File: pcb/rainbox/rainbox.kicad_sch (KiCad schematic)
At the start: 14 parts, among them J1 USB_C_Receptacle_USB2.0_14P, J2 Conn_01x04_Pin, U1 ESP32-S3-WROOM-2, U2 LM3940IMPX-3.3/NOPB, U3 ESC, U4 TMC2240_Module

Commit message: more kicad additions and research
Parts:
- added C6, C7: 0.1uF, symbol Device:C_Small
- added J3: Conn_01x02_Pin, symbol Connector:Conn_01x02_Pin
- added J4: Conn_01x02_Socket, Connector_PinSocket_2.54mm:PinSocket_1x02_P2.54mm_Vertical, symbol Connector:Conn_01x02_Socket
- added R4: 400Ω, symbol Device:R_Small
- added R5: 20kΩ, symbol Device:R_Small
- added U5, U6: WaterSensor_Module, Connector_PinHeader_2.54mm:PinHeader_1x03_P2.54mm_Vertical, symbol 1_udu_lib:Water_Sensor_Module
- added U7: Neopixel_Strip_Module, Connector_PinHeader_2.54mm:PinHeader_1x03_P2.54mm_Vertical, symbol 1_udu_lib:Neopixel_Strip_Module
- added U8: Ultrasonic_Atomizer_Module, Connector_PinHeader_2.54mm:PinHeader_1x03_P2.54mm_Vertical, symbol 1_udu_lib:Ultrasonic_Atomizer_Module
- added U9: TPS2113ADRBR, EasyEDA:SON-8_L3.0-W3.0-P0.65-LS3.0-BL-EP, symbol EasyEDA:TPS2113ADRBR
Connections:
- net +3.3V: now also U5.2 (3V3), U6.2 (3V3), U8.2 (3v3)
- net +5V: now also U7.2 (5v), U9.7 (OUT); no longer J1.A4 (VBUS), J1.A9 (VBUS), J1.B4 (VBUS), J1.B9 (VBUS)
- net D+: now also U1.14 (USB_D+/IO20)
- net D-: now also U1.13 (USB_D-/IO19)
- net GND: now also C6.1, C7.1, J3.1 (Pin_1), J4.2 (Pin_2), R4.1, R5.1, U5.3 (GND), U6.3 (GND), U7.3 (GND), U8.3 (GND), U9.2 (~{EN}), U9.5 (GND), U9.9 (EP); no longer U4.3 (EN)
- net DIR: now reaches U4.10 (DIR)
- net DIR: now also U1.6 (IO6)
- net at U4.18 (VM): now also J3.2 (Pin_2)
- net MOSI: now reaches U4.4 (MOSI)
- net MOSI: now also U1.18 (IO10)
- net SPI_CLK: now reaches U4.5 (SPI_CLK)
- net SPI_CLK: now also U1.19 (IO11)
- net CS: now reaches U4.6 (CS)
- net CS: now also U1.20 (IO12)
- net MISO: now reaches U4.7 (MISO)
- net MISO: now also U1.21 (IO13)
- net STEP: now reaches U4.9 (STEP)
- net STEP: now also U1.5 (IO5)
- net RGB: now reaches U1.12 (IO8)
- net RGB: now also U7.1 (Din)
- net Mist: now reaches U1.17 (IO9)
- net Mist: now also U8.1 (Signal)
- net S1Water: now reaches U1.38 (IO2)
- net S1Water: now also U5.1 (Signal)
- net ENABLE: now reaches U1.4 (IO4)
- net ENABLE: now also U4.3 (EN)
- net S2Water: now reaches U1.7 (IO7)
- net S2Water: now also U6.1 (Signal)
- new net: R4.2, U9.4 (ILIM)
- new net: R5.2, U9.3 (VSNS)
- new net 5V_BUCKDC: C7.2, J4.1 (Pin_1), U9.8 (IN1)
- new net 5V_VBUS: C6.2, J1.A4 (VBUS), J1.A9 (VBUS), J1.B4 (VBUS), J1.B9 (VBUS), U9.6 (IN2)
- no-connect marks 1 -> 8
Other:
- note added: "24v->5v dc dc buck converter"
- note added: "mist generator"
- note added: "neopixels"
- note added: "power management/mux"
- note added: "stepper motor"
- note added: "water sensors"
- moved on the sheet: J2

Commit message: update pcb
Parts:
- added C8, C9: 0.1uF, Capacitor_SMD:C_0603_1608Metric, symbol Device:C_Small
- added D1, D2: WS2812B, LED_SMD:LED_WS2812B_PLCC4_5.0x5.0mm_P3.2mm, symbol LED:WS2812B
- added SW1, SW2: SW_Push, Button_Switch_THT:SW_PUSH_6mm, symbol Switch:SW_Push
- added TP1, TP2, TP3: Mount Screw M3, MountingHole:MountingHole_3.2mm_M3_Pad_Via, symbol Connector:TestPoint
- added U10: USBLC6-2P6, Package_TO_SOT_SMD:SOT-666, symbol Power_Protection:USBLC6-2P6
- C1, C2, C3, C4, C5, C6, C7: footprint (none) -> Capacitor_SMD:C_0603_1608Metric
- J1: footprint (none) -> Snapeda:USB4105-GF-A_GCT_USB4105-GF-A
- J2: footprint (none) -> Connector_PinHeader_2.54mm:PinHeader_1x04_P2.54mm_Vertical
- J3: footprint (none) -> TerminalBlock_Phoenix:TerminalBlock_Phoenix_PT-1,5-2-5.0-H_1x02_P5.00mm_Horizontal
- R1, R2, R3, R4, R5: footprint (none) -> Resistor_SMD:R_0603_1608Metric
- U4: footprint (none) -> 1_udu_lib:tmc2240_module
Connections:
- net +3.3V: now also D1.1 (VDD), D2.1 (VDD)
- net 5V_VBUS: now also U10.5 (VBUS)
- net D+: now also U10.4 (I/O2); no longer J1.A6 (D+), J1.B6 (D+)
- net D-: now also U10.6 (I/O1); no longer J1.A7 (D-), J1.B7 (D-)
- net GND: now also C8.2, C9.2, D1.3 (VSS), D2.3 (VSS), SW1.2, SW2.2, TP1.1, TP2.1, TP3.1, U10.2 (GND)
- net EN_RESET: now reaches C3.2, R1.2, U1.3 (EN)
- net EN_RESET: now also C8.1, SW1.1
- net NEOPIXELS: now reaches U1.11 (IO18)
- net NEOPIXELS: now also D1.4 (DIN)
- net BOOT: now reaches U1.27 (IO0)
- net BOOT: now also C9.1, SW2.1
- new net: J1.A6 (D+), J1.B6 (D+), U10.3 (I/O2)
- new net: J1.A7 (D-), J1.B7 (D-), U10.1 (I/O1)
- new net: D1.2 (DOUT), D2.4 (DIN)
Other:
- note added: "boot and reset buttons"
- note added: "mounting screws"

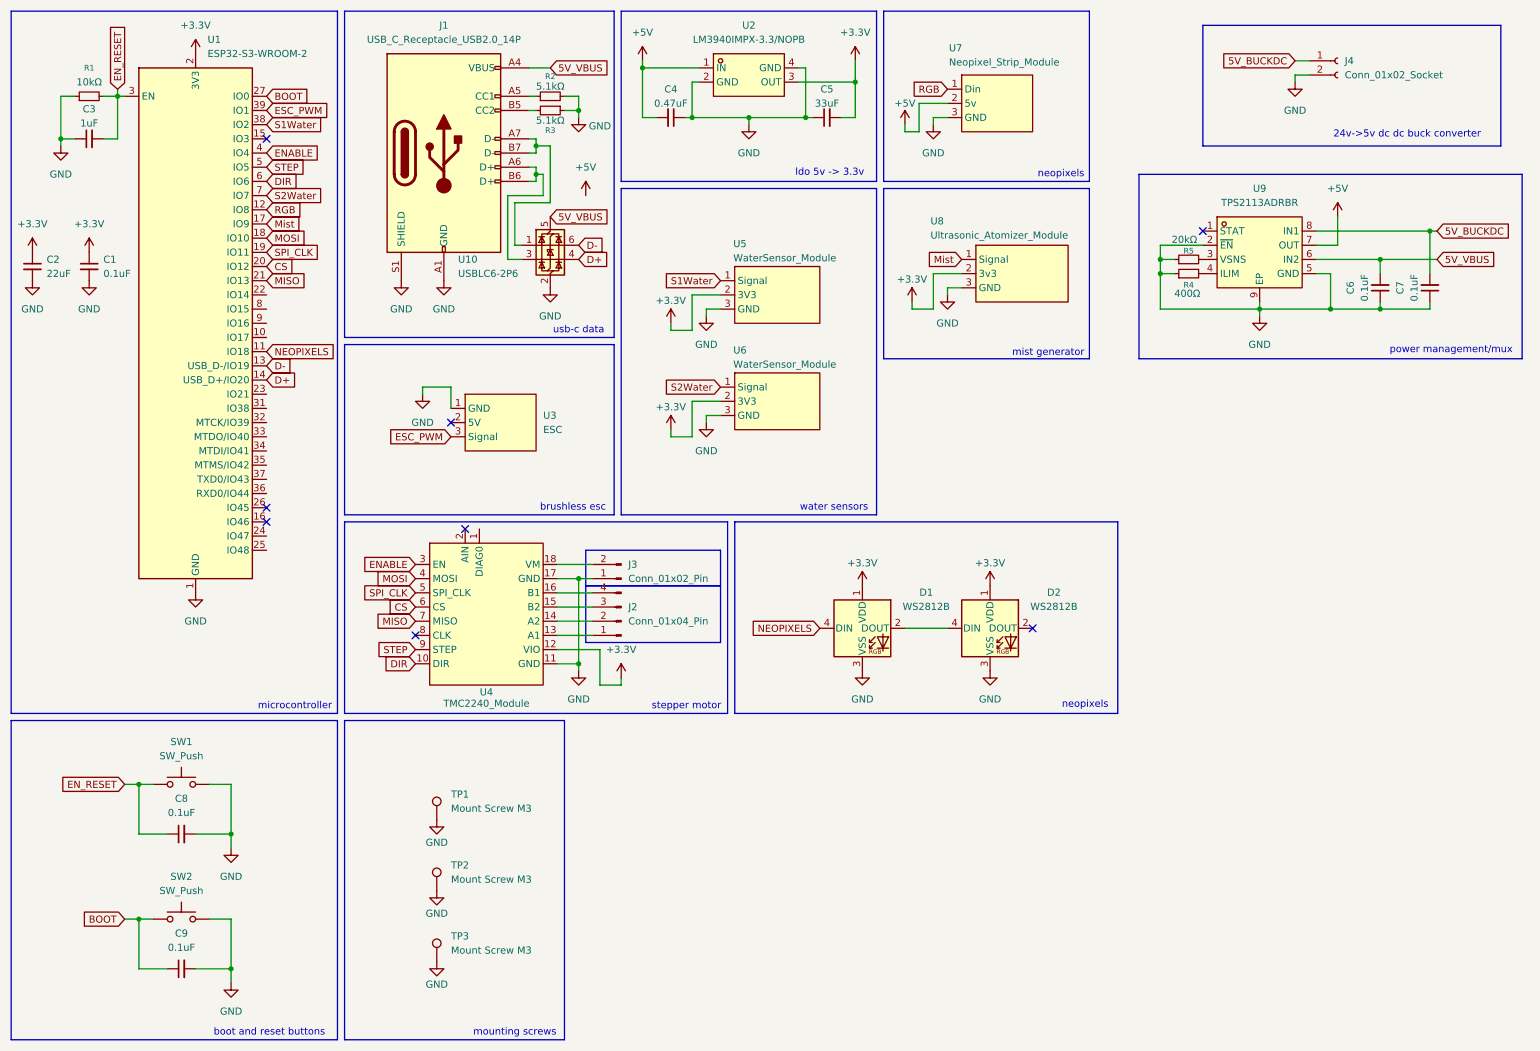
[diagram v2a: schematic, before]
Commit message: replace esc controller with dc motor ic
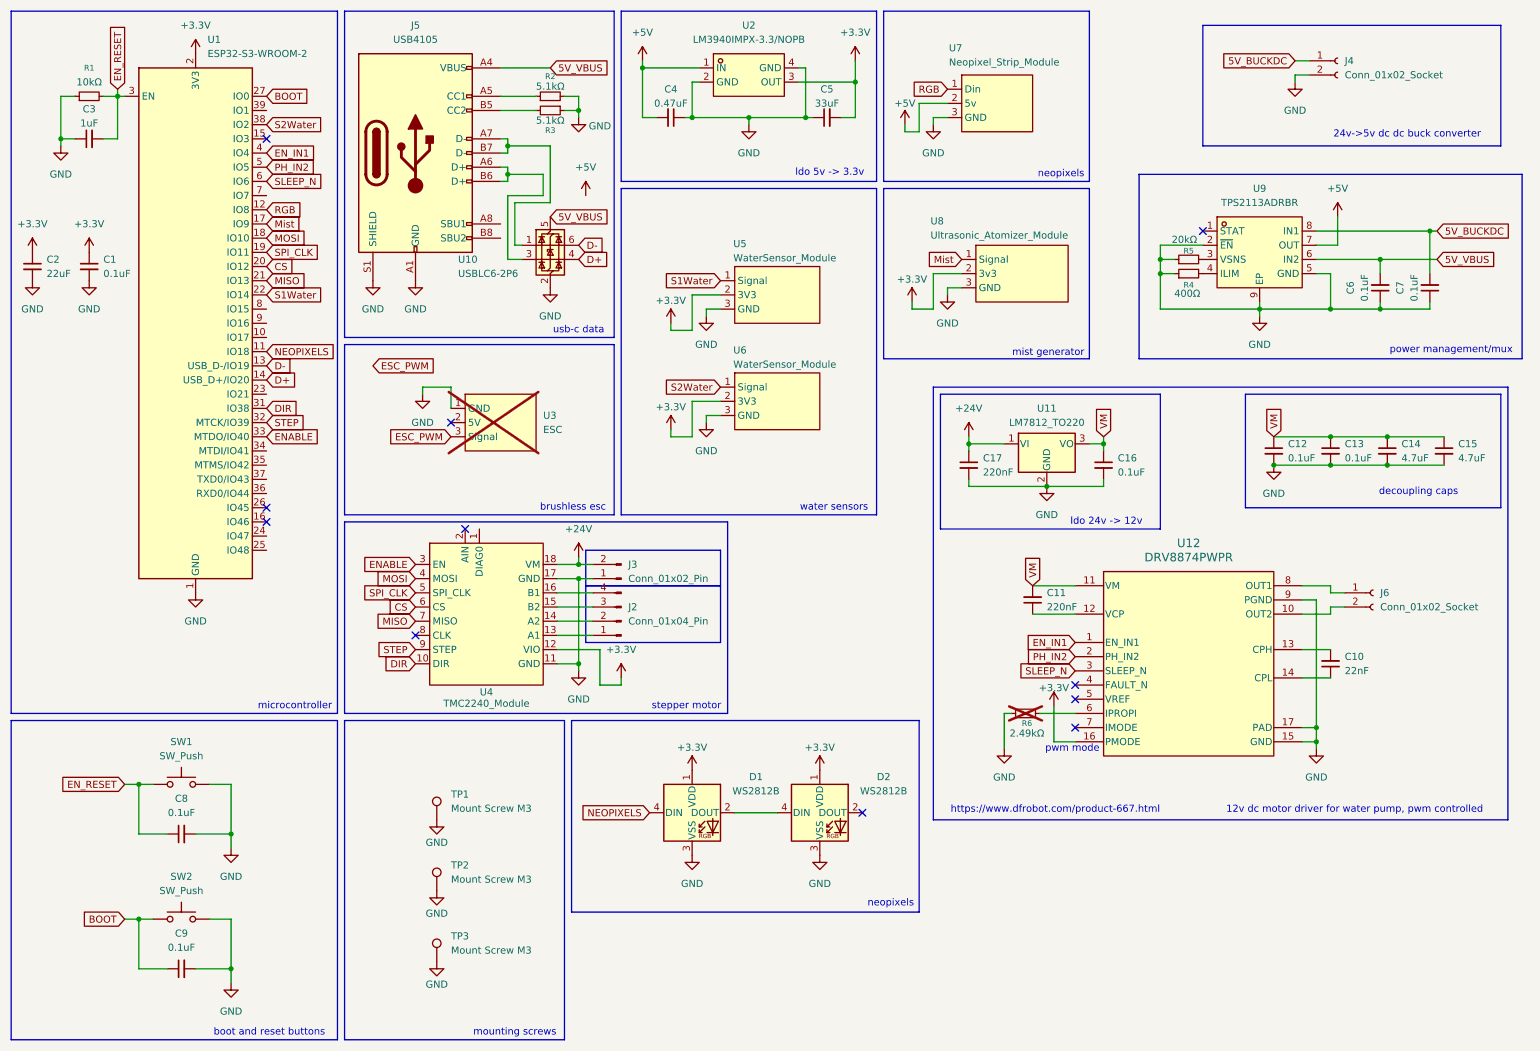
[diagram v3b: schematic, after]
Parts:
- removed J1: USB_C_Receptacle_USB2.0_14P, Snapeda:USB4105-GF-A_GCT_USB4105-GF-A, symbol Connector:USB_C_Receptacle_USB2.0_14P
- added C10: 22nF, Capacitor_SMD:C_0603_1608Metric, symbol Device:C_Small
- added C11, C17: 220nF, Capacitor_SMD:C_0603_1608Metric, symbol Device:C_Small
- added C12, C13, C16: 0.1uF, Capacitor_SMD:C_0603_1608Metric, symbol Device:C_Small
- added C14, C15: 4.7uF, Capacitor_SMD:C_0603_1608Metric, symbol Device:C_Small
- added J5: USB4105, Connector_USB:USB_C_Receptacle_GCT_USB4105-xx-A_16P_TopMnt_Horizontal, symbol Connector:USB_C_Receptacle_USB2.0_16P
- added J6: Conn_01x02_Socket, TerminalBlock_Phoenix:TerminalBlock_Phoenix_PT-1,5-2-5.0-H_1x02_P5.00mm_Horizontal, symbol Connector:Conn_01x02_Socket
- added R6: 2.49kΩ, Resistor_SMD:R_0603_1608Metric, symbol Device:R_Small
- added U11: LM7812_TO220, Package_TO_SOT_THT:TO-220-3_Vertical, symbol Regulator_Linear:LM7812_TO220
- added U12: DRV8874PWPR, 1_udu_lib:PWP0016J_N, symbol drv8874:DRV8874PWPR
- U3: now not fitted; now left out of the parts list
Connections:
- net +3.3V: now also U12.16 (PMODE)
- net 5V_VBUS: now also J5.A4 (VBUS), J5.A9 (VBUS), J5.B4 (VBUS), J5.B9 (VBUS)
- net DIR: now also U1.31 (IO38); no longer U1.6 (IO6)
- net ENABLE: now also U1.33 (MTDO/IO40); no longer U1.4 (IO4)
- net ESC_PWM: no longer U1.39 (IO1)
- net GND: now also C12.2, C13.2, C14.2, C15.2, C16.2, C17.2, J5.A1 (GND), J5.A12 (GND), J5.B1 (GND), J5.B12 (GND), J5.S1 (SHIELD), R6.1, U11.2 (GND), U12.15 (GND), U12.17 (PAD), U12.9 (PGND)
- net S1Water: now also U1.22 (IO14); no longer U1.38 (IO2)
- net S2Water: now also U1.38 (IO2); no longer U1.7 (IO7)
- net STEP: now also U1.32 (MTCK/IO39); no longer U1.5 (IO5)
- net +24V: now reaches J3.2 (Pin_2), U4.18 (VM)
- net +24V: now also C17.1, U11.1 (VI)
- net at R3.2: now also J5.B5 (CC2)
- net at R2.1: now also J5.A5 (CC1)
- net at U10.3 (I/O2): now also J5.A6 (D+), J5.B6 (D+)
- net at U10.1 (I/O1): now also J5.A7 (D-), J5.B7 (D-)
- new net: C10.1, U12.14 (CPL)
- new net: C10.2, U12.13 (CPH)
- new net: J6.1 (Pin_1), U12.8 (OUT1)
- new net: J6.2 (Pin_2), U12.10 (OUT2)
- new net: C11.1, U12.12 (VCP)
- new net: R6.2, U12.6 (IPROPI)
- new net EN_IN1: U1.4 (IO4), U12.1 (EN_IN1)
- new net PH_IN2: U1.5 (IO5), U12.2 (PH_IN2)
- new net SLEEP_N: U1.6 (IO6), U12.3 (SLEEP_N)
- new net VM: C11.2, C12.1, C13.1, C14.1, C15.1, C16.1, U11.3 (VO), U12.11 (VM)
- no-connect marks 8 -> 11
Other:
- note added: "12v dc motor driver for water pump, pwm controlled"
- note added: "decoupling caps"
- note added: "https://www.dfrobot.com/product-667.html"
- note added: "ldo 24v -> 12v"
- note added: "pwm mode"
- moved on the sheet: D1, D2

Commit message: pcb additions, readme, md stuff
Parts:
- C5: value 33uF -> 47uF
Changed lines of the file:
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@@
 			)
 		)
-		(property "Value" "33uF"
+		(property "Value" "47uF"
 			(at 158.7627 29.21 90)
 			(effects

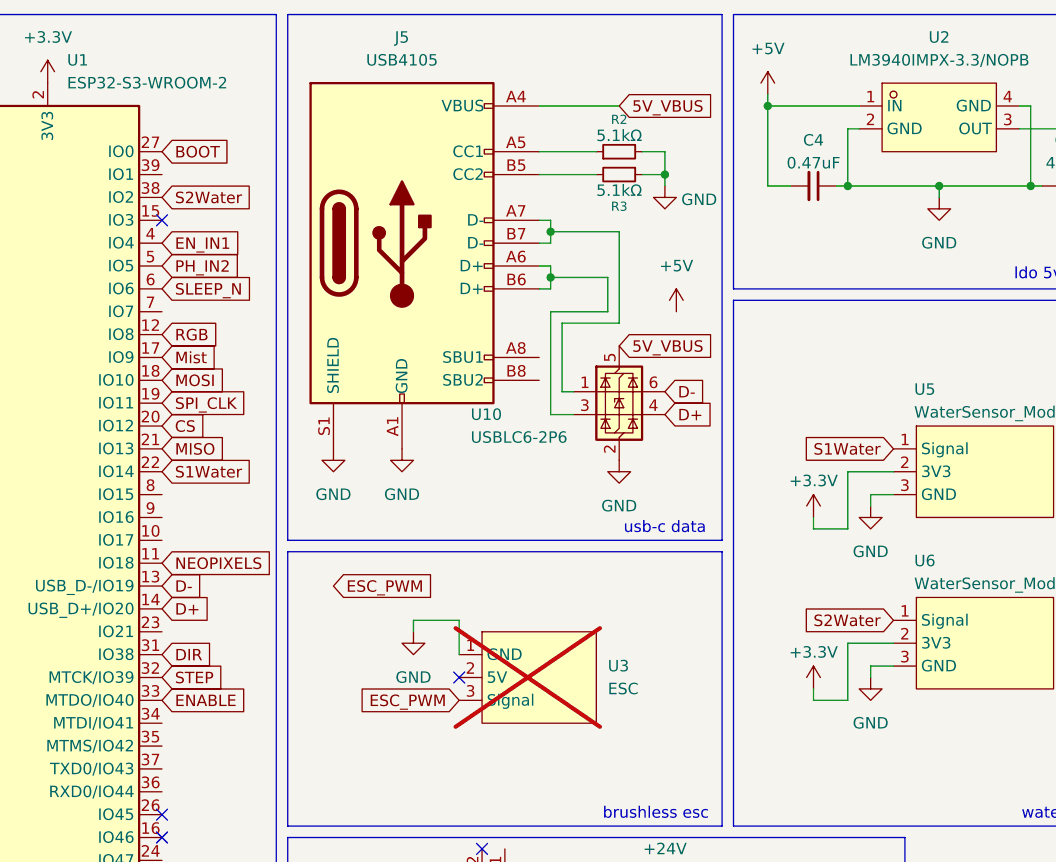
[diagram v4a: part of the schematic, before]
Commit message: add prototype firmware + fix pcb
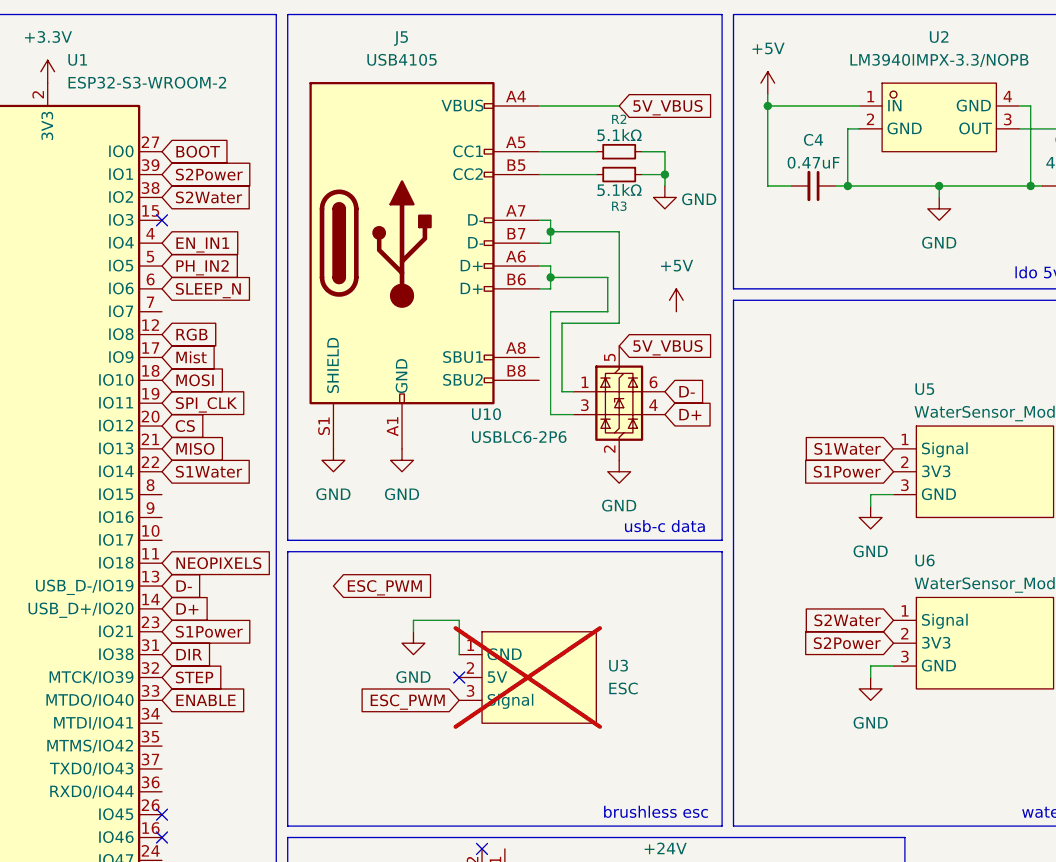
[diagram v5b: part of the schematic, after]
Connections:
- net +3.3V: no longer U5.2 (3V3), U6.2 (3V3)
- net S1Power: now reaches U1.23 (IO21)
- net S1Power: now also U5.2 (3V3)
- net S2Power: now reaches U1.39 (IO1)
- net S2Power: now also U6.2 (3V3)
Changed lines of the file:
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@@
 	(wire
 		(pts
-			(xy 130.81 69.85) (xy 130.81 68.58)
-		)
-		(stroke
-			(width 0)
-			(type default)
-		)
-	)
-	(wire
-		(pts
 			(xy 29.21 35.56) (xy 31.75 35.56)
 		)
@@
 	(wire
 		(pts
-			(xy 130.81 88.9) (xy 130.81 87.63)
-		)
-		(stroke
-			(width 0)
-			(type default)
-		)
-	)
-	(wire
-		(pts
 			(xy 144.78 33.02) (xy 144.78 31.75)
 		)
@@
 	(wire
 		(pts
-			(xy 134.62 63.5) (xy 134.62 69.85)
-		)
-		(stroke
-			(width 0)
-			(type default)
-		)
-	)
-	(wire
-		(pts
 			(xy 250.19 54.61) (xy 250.19 49.53)
 		)
@@
 	(wire
 		(pts
-			(xy 134.62 69.85) (xy 130.81 69.85)
-		)
-		(stroke
-			(width 0)
-			(type default)
-		)
-	)
-	(wire
-		(pts
 			(xy 149.86 156.21) (xy 142.24 156.21)
 		)
@@
 	(wire
 		(pts
-			(xy 139.7 63.5) (xy 134.62 63.5)
-		)
-		(stroke
-			(width 0)
-			(type default)
-		)
-	)
-	(wire
-		(pts
 			(xy 248.92 59.69) (xy 248.92 66.04)
 		)
@@
 	(wire
 		(pts
-			(xy 134.62 82.55) (xy 134.62 88.9)
-		)
-		(stroke
-			(width 0)
-			(type default)
-		)
-	)
-	(wire
-		(pts
 			(xy 21.59 35.56) (xy 21.59 27.94)
 		)
@@
 	(wire
 		(pts
-			(xy 134.62 88.9) (xy 130.81 88.9)
-		)
-		(stroke
-			(width 0)
-			(type default)
-		)
-	)
-	(wire
-		(pts
 			(xy 110.49 114.3) (xy 114.3 114.3)
 		)
@@
 	(wire
 		(pts
-			(xy 139.7 82.55) (xy 134.62 82.55)
-		)
-		(stroke
-			(width 0)
-			(type default)
-		)
-	)
-	(wire
-		(pts
 			(xy 248.92 93.98) (xy 259.08 93.98)
 		)
@@
 		)
 	)
+	(global_label "S2Power"
+		(shape input)
+		(at 58.42 30.48 0)
+		(fields_autoplaced yes)
+		(effects
+			(font
+				(size 1.27 1.27)
+			)
+			(justify left)
+		)
+		(property "Intersheetrefs" "${INTERSHEET_REFS}"
+			(at 69.4485 30.48 0)
+			(effects
+				(font
+					(size 1.27 1.27)
+				)
+				(justify left)
+				(hide yes)
+			)
+		)
+	)
 	(global_label "PH_IN2"
 		(shape input)
@@
 		)
 	)
+	(global_label "S2Power"
+		(shape input)
+		(at 139.7 82.55 180)
+		(fields_autoplaced yes)
+		(effects
+			(font
+				(size 1.27 1.27)
+			)
+			(justify right)
+		)
+		(property "Intersheetrefs" "${INTERSHEET_REFS}"
+			(at 128.6715 82.55 0)
+			(effects
+				(font
+					(size 1.27 1.27)
+				)
+				(justify right)
+				(hide yes)
+			)
+		)
+	)
 	(global_label "EN_IN1"
 		(shape input)
@@
 		)
 	)
+	(global_label "S1Power"
+		(shape input)
+		(at 139.7 63.5 180)
+		(fields_autoplaced yes)
+		(effects
+			(font
+				(size 1.27 1.27)
+			)
+			(justify right)
+		)
+		(property "Intersheetrefs" "${INTERSHEET_REFS}"
+			(at 128.6715 63.5 0)
+			(effects
+				(font
+					(size 1.27 1.27)
+				)
+				(justify right)
+				(hide yes)
+			)
+		)
+	)
 	(global_label "5V_BUCKDC"
 		(shape input)
@@
 		)
 	)
+	(global_label "S1Power"
+		(shape input)
+		(at 58.42 81.28 0)
+		(fields_autoplaced yes)
+		(effects
+			(font
+				(size 1.27 1.27)
+			)
+			(justify left)
+		)
+		(property "Intersheetrefs" "${INTERSHEET_REFS}"
+			(at 69.4485 81.28 0)
+			(effects
+				(font
+					(size 1.27 1.27)
+				)
+				(justify left)
+				(hide yes)
+			)
+		)
+	)
 	(global_label "VM"
 		(shape input)
@@
 	)
 	(symbol
-		(lib_id "power:+3.3V")
-		(at 130.81 68.58 0)
-		(unit 1)
-		(exclude_from_sim no)
-		(in_bom yes)
-		(on_board yes)
-		(dnp no)
-		(property "Reference" "#PWR019"
-			(at 130.81 72.39 0)
-			(effects
-				(font
-					(size 1.27 1.27)
-				)
-				(hide yes)
-			)
-		)
-		(property "Value" "+3.3V"
-			(at 130.81 64.516 0)
-			(effects
-				(font
-					(size 1.27 1.27)
-				)
-			)
-		)
-		(property "Footprint" ""
-			(at 130.81 68.58 0)
-			(effects
-				(font
-					(size 1.27 1.27)
-				)
-				(hide yes)
-			)
-		)
-		(property "Datasheet" ""
-			(at 130.81 68.58 0)
-			(effects
-				(font
-					(size 1.27 1.27)
-				)
-				(hide yes)
-			)
-		)
-		(property "Description" "Power symbol creates a global label with name \"+3.3V\""
-			(at 130.81 68.58 0)
-			(effects
-				(font
-					(size 1.27 1.27)
-				)
-				(hide yes)
-			)
-		)
-		(pin "1"
-		)
-		(instances
-			(project "rainbox"
-				(path "/dd609afc-35f2-4e8c-9510-83a0786896a4"
-					(reference "#PWR019")
-					(unit 1)
-				)
-			)
-		)
-	)
-	(symbol
 		(lib_id "1_udu_lib:Water_Sensor_Module")
 		(at 149.86 63.5 0)
@@
 					(unit 1)
 				)
-			)
-		)
-	)
-	(symbol
-		(lib_id "power:+3.3V")
-		(at 130.81 87.63 0)
-		(unit 1)
-		(exclude_from_sim no)
-		(in_bom yes)
-		(on_board yes)
-		(dnp no)
-		(property "Reference" "#PWR020"
-			(at 130.81 91.44 0)
-			(effects
-				(font
-					(size 1.27 1.27)
-				)
-				(hide yes)
-			)
-		)
-		(property "Value" "+3.3V"
-			(at 130.81 83.566 0)
-			(effects
-				(font
-					(size 1.27 1.27)
-				)
-			)
-		)
-		(property "Footprint" ""
-			(at 130.81 87.63 0)
-			(effects
-				(font
-					(size 1.27 1.27)
-				)
-				(hide yes)
-			)
-		)
-		(property "Datasheet" ""
-			(at 130.81 87.63 0)
-			(effects
-				(font
-					(size 1.27 1.27)
-				)
-				(hide yes)
-			)
-		)
-		(property "Description" "Power symbol creates a global label with name \"+3.3V\""
-			(at 130.81 87.63 0)
-			(effects
-				(font
-					(size 1.27 1.27)
-				)
-				(hide yes)
-			)
-		)
-		(pin "1"
-		)
-		(instances
-			(project "rainbox"
-				(path "/dd609afc-35f2-4e8c-9510-83a0786896a4"
-					(reference "#PWR020")
-					(unit 1)
-				)
